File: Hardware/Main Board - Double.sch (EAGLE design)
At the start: 69 parts, among them J1 MICROMOD-2222-C, J10 MICRO-SD-PUSH-PUSH-EXT-PIN, J2 Vertical Qwiic Connector, J4 QWIIC_RIGHT_ANGLE, J5 CORTEX_JTAG_DEBUG_MINIMUM_PTH, J6 MICROMOD_CARRIER, J7 MICROMOD_CARRIER, Q1 3.1A/30V/105mΩ, U2 MCP73831, U5 AP7361C-33

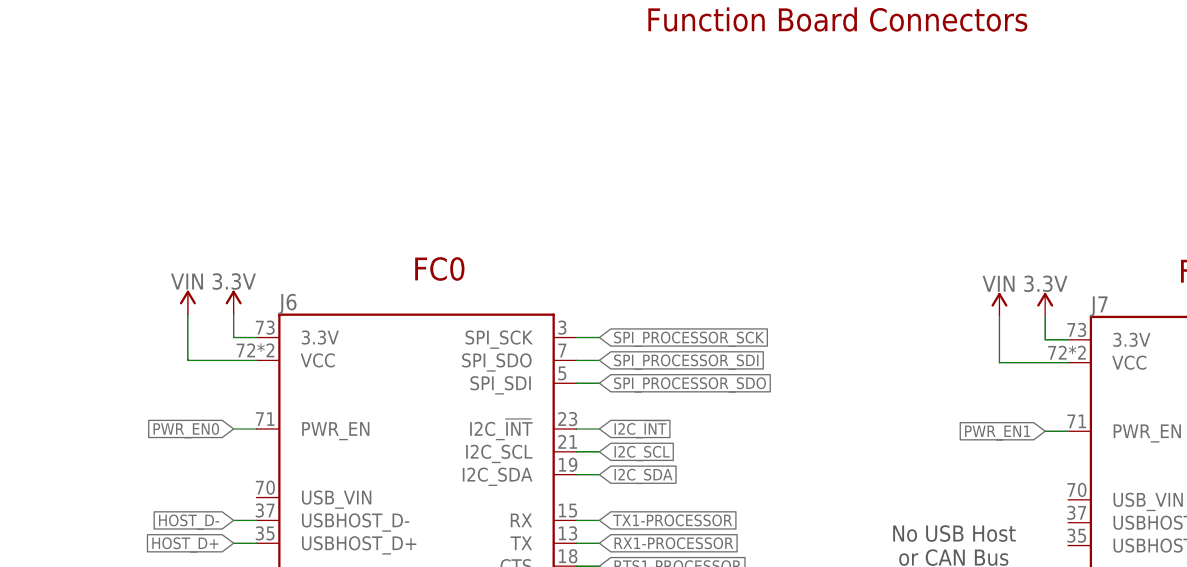
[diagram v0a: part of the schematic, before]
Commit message: Changes power to Function Boards @ VCC to VCC rather than VIN
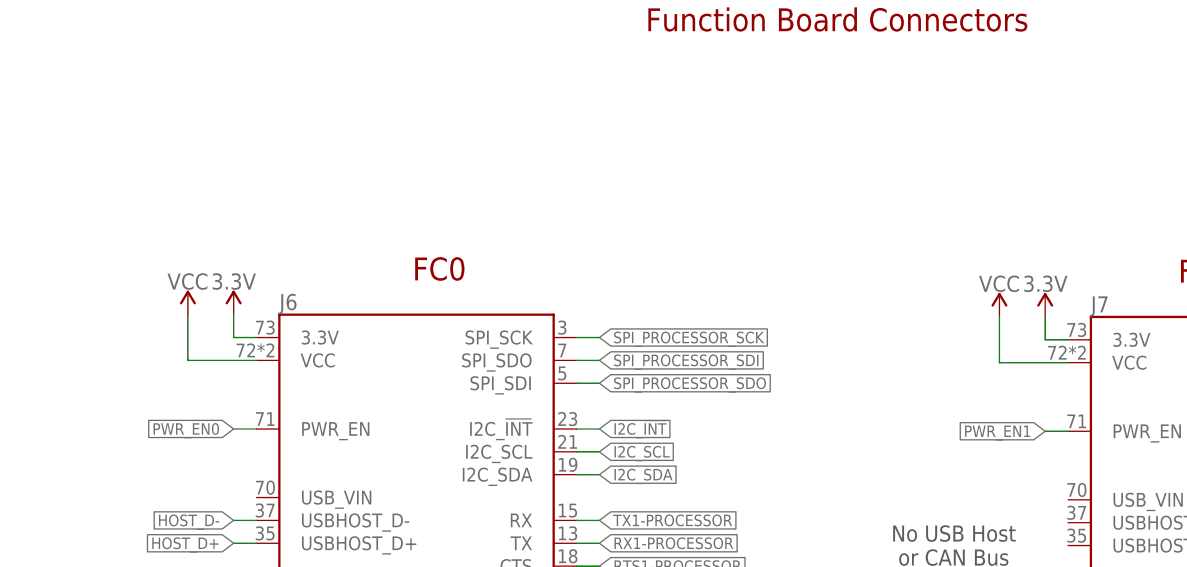
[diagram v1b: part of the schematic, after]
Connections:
- net VCC: now also J6.VCC, J7.VCC
- net VIN: no longer J6.VCC, J7.VCC
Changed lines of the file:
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@@
 <part name="H4" library="SparkFun-Hardware" deviceset="STAND-OFF-REFLOW" device="-M2.5_2.5MM_TALL"/>
 <part name="GND40" library="SparkFun-PowerSymbols" deviceset="GND" device=""/>
-<part name="SUPPLY9" library="SparkFun-PowerSymbols" deviceset="VIN" device=""/>
-<part name="SUPPLY23" library="SparkFun-PowerSymbols" deviceset="VIN" device=""/>
 <part name="SUPPLY4" library="SparkFun-PowerSymbols" deviceset="VIN" device=""/>
 <part name="LOGO2" library="SparkFun-Aesthetics" deviceset="SFE_LOGO_NAME_FLAME" device=".3_INCH"/>
@@
 <part name="J9" library="SparkFun-Connectors" deviceset="CONN_03" device="LOCK"/>
 <part name="J11" library="SparkFun-Connectors" deviceset="CONN_03" device="LOCK"/>
+<part name="SUPPLY8" library="SparkFun-PowerSymbols" deviceset="VCC" device=""/>
+<part name="SUPPLY9" library="SparkFun-PowerSymbols" deviceset="VCC" device=""/>
 </parts>
 <sheets>
@@
 <attribute name="VALUE" x="195.58" y="7.366" size="1.778" layer="96" font="vector" align="top-center"/>
 </instance>
-<instance part="SUPPLY9" gate="G$1" x="24.638" y="91.186" smashed="yes">
-<attribute name="VALUE" x="24.638" y="93.98" size="1.778" layer="96" align="bottom-center"/>
-</instance>
-<instance part="SUPPLY23" gate="G$1" x="114.808" y="90.932" smashed="yes">
-<attribute name="VALUE" x="114.808" y="93.726" size="1.778" layer="96" align="bottom-center"/>
-</instance>
 <instance part="SUPPLY4" gate="G$1" x="13.716" y="178.562" smashed="yes">
 <attribute name="VALUE" x="13.716" y="181.356" size="1.778" layer="96" align="bottom-center"/>
@@
 <attribute name="VALUE" x="182.88" y="187.706" size="1.778" layer="96" font="vector" rot="R180"/>
 <attribute name="NAME" x="182.88" y="174.752" size="1.778" layer="95" font="vector" rot="R180"/>
+</instance>
+<instance part="SUPPLY8" gate="G$1" x="114.808" y="90.932" smashed="yes">
+<attribute name="VALUE" x="114.808" y="93.726" size="1.778" layer="96" align="bottom-center"/>
+</instance>
+<instance part="SUPPLY9" gate="G$1" x="24.638" y="91.186" smashed="yes">
+<attribute name="VALUE" x="24.638" y="93.98" size="1.778" layer="96" align="bottom-center"/>
 </instance>
 </instances>
@@
 </net>
 <net name="VIN" class="0">
-<segment>
-<pinref part="SUPPLY9" gate="G$1" pin="VIN"/>
-<wire x1="24.638" y1="86.106" x2="24.638" y2="91.186" width="0.1524" layer="91"/>
-<pinref part="J6" gate="J1" pin="VCC"/>
-<wire x1="32.258" y1="86.106" x2="24.638" y2="86.106" width="0.1524" layer="91"/>
-</segment>
-<segment>
-<pinref part="SUPPLY23" gate="G$1" pin="VIN"/>
-<wire x1="114.808" y1="85.852" x2="114.808" y2="90.932" width="0.1524" layer="91"/>
-<pinref part="J7" gate="J1" pin="VCC"/>
-<wire x1="122.428" y1="85.852" x2="114.808" y2="85.852" width="0.1524" layer="91"/>
-</segment>
 <segment>
 <pinref part="R10" gate="G$1" pin="2"/>
@@
 <pinref part="SUPPLY6" gate="G$1" pin="VCC"/>
 </segment>
-</net>
+<segment>
+<wire x1="24.638" y1="86.106" x2="24.638" y2="91.186" width="0.1524" layer="91"/>
+<pinref part="J6" gate="J1" pin="VCC"/>
+<wire x1="32.258" y1="86.106" x2="24.638" y2="86.106" width="0.1524" layer="91"/>
+<pinref part="SUPPLY9" gate="G$1" pin="VCC"/>
+</segment>
+<segment>
+<wire x1="114.808" y1="85.852" x2="114.808" y2="90.932" width="0.1524" layer="91"/>
+<pinref part="J7" gate="J1" pin="VCC"/>
+<wire x1="122.428" y1="85.852" x2="114.808" y2="85.852" width="0.1524" layer="91"/>
+<pinref part="SUPPLY8" gate="G$1" pin="VCC"/>
+</segment>
+</net>

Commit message: Rolls to v11
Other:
- note added: "v11"
- note removed: "v10"
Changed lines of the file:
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@@
 <text x="96.774" y="123.952" size="2.54" layer="94" font="vector" align="center">Function Board Connectors</text>
 <text x="95.25" y="271.526" size="2.54" layer="94" font="vector" align="center">Processor Board Connector</text>
-<text x="424.18" y="7.62" size="2.54" layer="94" font="vector" align="center">v10</text>
+<text x="424.18" y="7.62" size="2.54" layer="94" font="vector" align="center">v11</text>
 <wire x1="330.2" y1="132.08" x2="274.32" y2="132.08" width="0.2032" layer="97" style="longdash"/>
 <wire x1="274.32" y1="132.08" x2="205.74" y2="132.08" width="0.2032" layer="97" style="longdash"/>

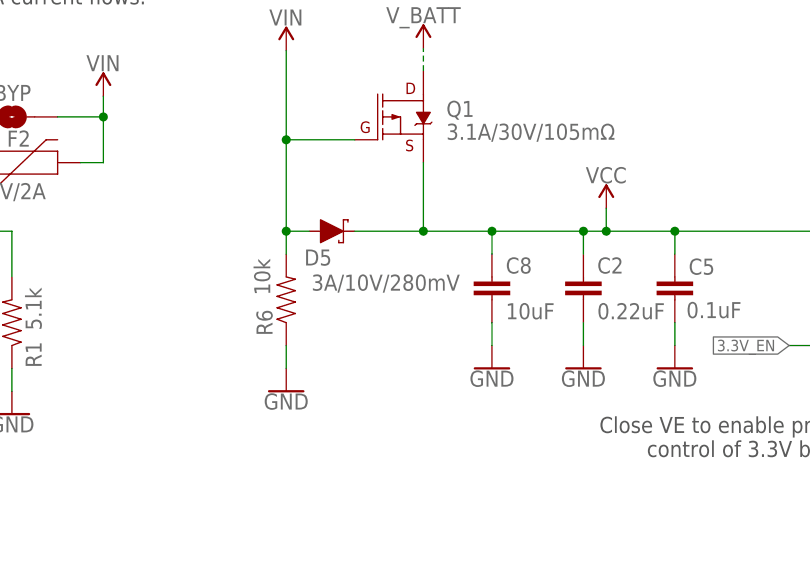
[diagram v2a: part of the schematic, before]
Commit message: Replaces schottky diode
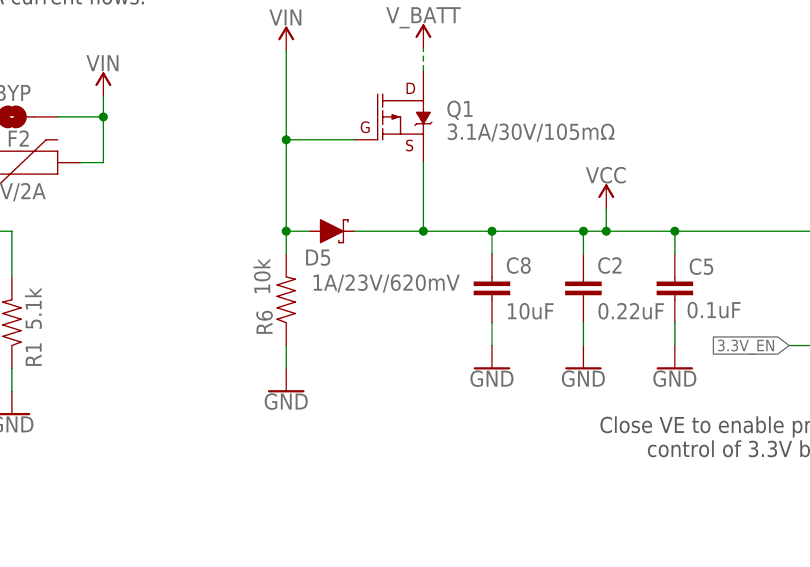
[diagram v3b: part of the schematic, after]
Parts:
- D5: value 3A/10V/280mV -> 1A/23V/620mV; device SparkFun-DiscreteSemi:DIODE-SCHOTTKY-BAT60A -> SparkFun-DiscreteSemi:DIODE-SCHOTTKY-BAT20J
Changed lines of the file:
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@@
 <part name="SUPPLY28" library="SparkFun-PowerSymbols" deviceset="VCC" device=""/>
 <part name="SUPPLY6" library="SparkFun-PowerSymbols" deviceset="VCC" device=""/>
-<part name="D5" library="SparkFun-DiscreteSemi" deviceset="DIODE-SCHOTTKY" device="-BAT60A" value="3A/10V/280mV"/>
+<part name="D5" library="SparkFun-DiscreteSemi" deviceset="DIODE-SCHOTTKY" device="-BAT20J" value="1A/23V/620mV"/>
 <part name="5V_LED" library="SparkFun-Jumpers" deviceset="JUMPER-SMT_2_NC_TRACE" device="_SILK" package3d_urn="urn:adsk.eagle:package:39281/1" value=""/>
 <part name="R8" library="SparkFun-Resistors" deviceset="4.7KOHM" device="-0603-1/10W-1%" value="4.7k"/>

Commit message: Updates Function board symbol, fixes some text explaining two pin jumper, corrects charging current.
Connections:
- net !CS0!-PROCESSOR: now also J6.F1/!CS!; no longer J6.G1/!CS!
- net !CS1!-PROCESSOR: now also J7.F1/!CS!; no longer J7.G1/!CS!
- net D0-PROCESSOR: now also J6.F0/!INT!; no longer J6.G0/!INT!
- net D1-PROCESSOR: now also J7.F0/!INT!; no longer J7.G0/!INT!
- net G0-PROCESSOR: now also J6.F3; no longer J6.G3
- net G1-PROCESSOR: now also J6.F4; no longer J6.G4
- net G2-PROCESSOR: now also J6.F5; no longer J6.G5
- net G3-PROCESSOR: now also J6.F6; no longer J6.G6
- net G4-PROCESSOR/SD_CARD_!CS!: now also J6.F7; no longer J6.G7
- net G5-PROCESSOR: now also J7.F3; no longer J7.G3
- net G6-PROCESSOR: now also J7.F4; no longer J7.G4
- net G7-PROCESSOR: now also J7.F5; no longer J7.G5
- net G8-PROCESSOR: now also J7.F6; no longer J7.G6
- net G9-PROCESSOR: now also J7.F7; no longer J7.G7
- net PWM0-PROCESSOR: now also J6.F2/PWM; no longer J6.G2/PWM
- net PWM1-PROCESSOR: now also J7.F2/PWM; no longer J7.G2/PWM
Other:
- note added: "600mA"
- note added: "Certain processors have limited GPIO and so these alternative power enable pins have been provided. Simply move the 2-pin Jumper to suit your project's needs."
- note removed: "166mA"
- note removed: "Certain processors have limited GPIO and so these alternative power enable pins have been provided. Simply move the shunt to suit your project's needs."
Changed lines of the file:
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@@
 <part name="GND34" library="SparkFun-PowerSymbols" deviceset="GND" device=""/>
 <part name="GND35" library="SparkFun-PowerSymbols" deviceset="GND" device=""/>
-<part name="VE" library="SparkFun-Jumpers" deviceset="JUMPER-SMT_2_NO" device="_SILK" package3d_urn="urn:adsk.eagle:package:39279/1" value=""/>
-<part name="3V3_LED" library="SparkFun-Jumpers" deviceset="JUMPER-SMT_2_NC_TRACE" device="_SILK" package3d_urn="urn:adsk.eagle:package:39281/1" value=""/>
+<part name="VE" library="SparkFun-Jumpers" deviceset="JUMPER-SMT_2_NO" device="_SILK" package3d_urn="urn:adsk.eagle:package:39279/1" value="JUMPER-SMT_2_NO_SILK"/>
+<part name="3V3_LED" library="SparkFun-Jumpers" deviceset="JUMPER-SMT_2_NC_TRACE" device="_SILK" package3d_urn="urn:adsk.eagle:package:39281/1" value="JUMPER-SMT_2_NC_TRACE_SILK"/>
 <part name="R11" library="SparkFun-Resistors" deviceset="1KOHM" device="-0603-1/10W-1%" value="1k"/>
 <part name="D3" library="SparkFun-LED" deviceset="LED-RED" device="0603" value="RED"/>
@@
 <part name="SUPPLY6" library="SparkFun-PowerSymbols" deviceset="VCC" device=""/>
 <part name="D5" library="SparkFun-DiscreteSemi" deviceset="DIODE-SCHOTTKY" device="-BAT20J" value="1A/23V/620mV"/>
-<part name="5V_LED" library="SparkFun-Jumpers" deviceset="JUMPER-SMT_2_NC_TRACE" device="_SILK" package3d_urn="urn:adsk.eagle:package:39281/1" value=""/>
+<part name="5V_LED" library="SparkFun-Jumpers" deviceset="JUMPER-SMT_2_NC_TRACE" device="_SILK" package3d_urn="urn:adsk.eagle:package:39281/1" value="JUMPER-SMT_2_NC_TRACE_SILK"/>
 <part name="R8" library="SparkFun-Resistors" deviceset="4.7KOHM" device="-0603-1/10W-1%" value="4.7k"/>
 <part name="D8" library="SparkFun-LED" deviceset="LED-RED" device="0603" value="RED"/>
@@
 <wire x1="391.16" y1="144.78" x2="424.18" y2="144.78" width="0.2032" layer="97"/>
 <text x="393.7" y="139.7" size="2.54" layer="97" font="vector">1+2</text>
-<text x="406.4" y="139.7" size="2.54" layer="97" font="vector">166mA</text>
 <wire x1="365.76" y1="152.4" x2="388.62" y2="152.4" width="0.2032" layer="97" style="dashdot"/>
 <wire x1="182.88" y1="0" x2="182.88" y2="27.94" width="0.2032" layer="97" style="longdash"/>
@@
 <text x="134.62" y="192.278" size="1.778" layer="97" font="vector">Certain processors have limited GPIO and
 so these alternative power enable pins have
-been provided. Simply move the shunt to
-suit your project's needs.
+been provided. Simply move the 2-pin
+Jumper to suit your project's needs.
 </text>
 <wire x1="154.94" y1="180.34" x2="147.32" y2="180.34" width="0.1524" layer="97" style="dashdot"/>
@@
 <text x="143.764" y="216.408" size="1.778" layer="97" font="vector">Default</text>
 <text x="146.558" y="181.102" size="1.778" layer="97" font="vector">Default</text>
+<text x="406.4" y="139.7" size="2.54" layer="97" font="vector">600mA</text>
 </plain>
 <instances>
@@
 <instance part="3V3_LED" gate="G$1" x="239.776" y="22.606" smashed="yes" rot="R90">
 <attribute name="NAME" x="237.744" y="17.78" size="1.778" layer="95" font="vector" rot="R90"/>
-<attribute name="VALUE" x="242.316" y="12.446" size="1.778" layer="96" font="vector" rot="R90" align="top-left"/>
 </instance>
 <instance part="R11" gate="G$1" x="239.776" y="45.466" smashed="yes" rot="R90">
@@
 <instance part="5V_LED" gate="G$1" x="227.076" y="22.606" smashed="yes" rot="R90">
 <attribute name="NAME" x="224.79" y="17.526" size="1.778" layer="95" font="vector" rot="R90"/>
-<attribute name="VALUE" x="229.616" y="12.446" size="1.778" layer="96" font="vector" rot="R90" align="top-left"/>
 </instance>
 <instance part="R8" gate="G$1" x="227.076" y="45.466" smashed="yes" rot="R90">
@@
 <wire x1="67.818" y1="42.926" x2="70.358" y2="42.926" width="0.1524" layer="91"/>
 <label x="70.358" y="42.926" size="1.27" layer="95" font="vector" xref="yes"/>
-<pinref part="J6" gate="J1" pin="G3"/>
+<pinref part="J6" gate="J1" pin="F3"/>
 </segment>
 <segment>
@@
 <wire x1="67.818" y1="40.386" x2="70.358" y2="40.386" width="0.1524" layer="91"/>
 <label x="70.358" y="40.386" size="1.27" layer="95" font="vector" xref="yes"/>
-<pinref part="J6" gate="J1" pin="G4"/>
+<pinref part="J6" gate="J1" pin="F4"/>
 </segment>
 <segment>
@@
 <wire x1="67.818" y1="37.846" x2="70.358" y2="37.846" width="0.1524" layer="91"/>
 <label x="70.358" y="37.846" size="1.27" layer="95" font="vector" xref="yes"/>
-<pinref part="J6" gate="J1" pin="G5"/>
+<pinref part="J6" gate="J1" pin="F5"/>
 </segment>
 </net>
@@
 <wire x1="67.818" y1="35.306" x2="70.358" y2="35.306" width="0.1524" layer="91"/>
 <label x="70.358" y="35.306" size="1.27" layer="95" font="vector" xref="yes"/>
-<pinref part="J6" gate="J1" pin="G6"/>
+<pinref part="J6" gate="J1" pin="F6"/>
 </segment>
 </net>
@@
 <wire x1="67.818" y1="32.766" x2="70.358" y2="32.766" width="0.1524" layer="91"/>
 <label x="70.358" y="32.766" size="1.27" layer="95" font="vector" xref="yes"/>
-<pinref part="J6" gate="J1" pin="G7"/>
+<pinref part="J6" gate="J1" pin="F7"/>
 </segment>
 </net>
@@
 </segment>
 <segment>
-<pinref part="J6" gate="J1" pin="G1/!CS!"/>
+<pinref part="J6" gate="J1" pin="F1/!CS!"/>
 <wire x1="67.818" y1="48.006" x2="70.358" y2="48.006" width="0.1524" layer="91"/>
 <label x="70.358" y="48.006" size="1.27" layer="95" font="vector" xref="yes"/>
@@
 <net name="!CS1!-PROCESSOR" class="0">
 <segment>
-<pinref part="J7" gate="J1" pin="G1/!CS!"/>
+<pinref part="J7" gate="J1" pin="F1/!CS!"/>
 <wire x1="157.988" y1="47.752" x2="160.528" y2="47.752" width="0.1524" layer="91"/>
 <label x="160.528" y="47.752" size="1.27" layer="95" font="vector" xref="yes"/>
@@
 </segment>
 <segment>
-<pinref part="J6" gate="J1" pin="G0/!INT!"/>
+<pinref part="J6" gate="J1" pin="F0/!INT!"/>
 <wire x1="67.818" y1="50.546" x2="70.358" y2="50.546" width="0.1524" layer="91"/>
 <label x="70.358" y="50.546" size="1.27" layer="95" font="vector" xref="yes"/>
@@
 </segment>
 <segment>
-<pinref part="J7" gate="J1" pin="G0/!INT!"/>
+<pinref part="J7" gate="J1" pin="F0/!INT!"/>
 <wire x1="157.988" y1="50.292" x2="160.528" y2="50.292" width="0.1524" layer="91"/>
 <label x="160.528" y="50.292" size="1.27" layer="95" font="vector" xref="yes"/>
@@
 <wire x1="157.988" y1="42.672" x2="160.528" y2="42.672" width="0.1524" layer="91"/>
 <label x="160.528" y="42.672" size="1.27" layer="95" font="vector" xref="yes"/>
-<pinref part="J7" gate="J1" pin="G3"/>
+<pinref part="J7" gate="J1" pin="F3"/>
 </segment>
 <segment>
@@
 <wire x1="157.988" y1="40.132" x2="160.528" y2="40.132" width="0.1524" layer="91"/>
 <label x="160.528" y="40.132" size="1.27" layer="95" font="vector" xref="yes"/>
-<pinref part="J7" gate="J1" pin="G4"/>
+<pinref part="J7" gate="J1" pin="F4"/>
 </segment>
 <segment>
@@
 <wire x1="157.988" y1="37.592" x2="160.528" y2="37.592" width="0.1524" layer="91"/>
 <label x="160.528" y="37.592" size="1.27" layer="95" font="vector" xref="yes"/>
-<pinref part="J7" gate="J1" pin="G5"/>
+<pinref part="J7" gate="J1" pin="F5"/>
 </segment>
 </net>
@@
 <wire x1="157.988" y1="35.052" x2="160.528" y2="35.052" width="0.1524" layer="91"/>
 <label x="160.528" y="35.052" size="1.27" layer="95" font="vector" xref="yes"/>
-<pinref part="J7" gate="J1" pin="G6"/>
+<pinref part="J7" gate="J1" pin="F6"/>
 </segment>
 <segment>
@@
 </segment>
 <segment>
-<pinref part="J7" gate="J1" pin="G2/PWM"/>
+<pinref part="J7" gate="J1" pin="F2/PWM"/>
 <wire x1="157.988" y1="45.212" x2="160.528" y2="45.212" width="0.1524" layer="91"/>
 <label x="160.528" y="45.212" size="1.27" layer="95" font="vector" xref="yes"/>
@@
 </segment>
 <segment>
-<pinref part="J6" gate="J1" pin="G2/PWM"/>
+<pinref part="J6" gate="J1" pin="F2/PWM"/>
 <wire x1="67.818" y1="45.466" x2="70.358" y2="45.466" width="0.1524" layer="91"/>
 <label x="70.358" y="45.466" size="1.27" layer="95" font="vector" xref="yes"/>
@@
 <wire x1="157.988" y1="32.512" x2="160.528" y2="32.512" width="0.1524" layer="91"/>
 <label x="160.528" y="32.512" size="1.27" layer="95" font="vector" xref="yes"/>
-<pinref part="J7" gate="J1" pin="G7"/>
-</segment>
-<segment>
+<pinref part="J7" gate="J1" pin="F7"/>
+</segment>
+<segment>
